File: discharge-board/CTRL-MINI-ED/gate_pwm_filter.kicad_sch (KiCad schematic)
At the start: 3 parts, among them U8 BD33FC0FP

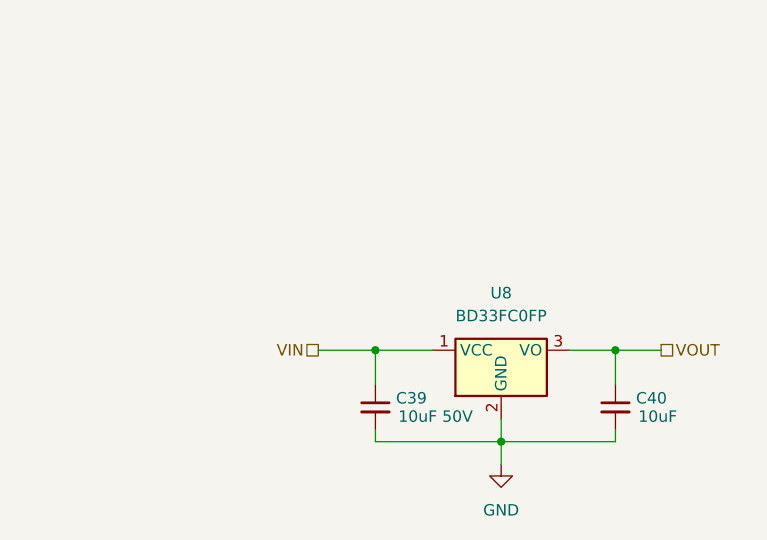
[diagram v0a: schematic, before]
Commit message: Add PWM voltage divider and refactor
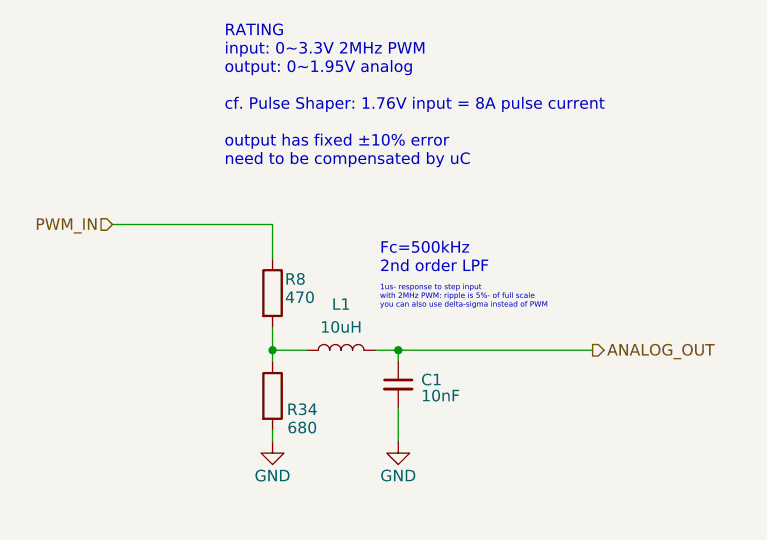
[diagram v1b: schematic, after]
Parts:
- removed C39: 10uF 50V, Capacitor_SMD:C_1206_3216Metric, symbol Device:C_Small
- removed C40: 10uF, Capacitor_SMD:C_0603_1608Metric, symbol Device:C_Small
- removed U8: BD33FC0FP, Package_TO_SOT_SMD:TO-252-2, symbol Regulator_Linear:BD33FC0FP
- added C1: 10nF, Capacitor_SMD:C_0603_1608Metric, symbol Device:C_Small
- added L1: 10uH, Inductor_SMD:L_0603_1608Metric, symbol Device:L
- added R34: 680, Resistor_SMD:R_0603_1608Metric, symbol Device:R
- added R8: 470, Resistor_SMD:R_0603_1608Metric, symbol Device:R
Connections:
- net GND: now also C1.2, R34.2
- new net: L1.1, R34.1, R8.2
- new net ANALOG_OUT: C1.1, L1.2
- new net PWM_IN: R8.1
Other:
- note added: "1us- response to step input with 2MHz PWM: ripple is 5%- of full scale you can also use delta-sigma instead of PWM"
- note added: "Fc=500kHz 2nd order LPF"
- note added: "RATING input: 0~3.3V 2MHz PWM output: 0~1.95V analog cf. Pulse Shaper: 1.76V input = 8A pulse current output has fixed ±10% error need to be compensated by uC"
